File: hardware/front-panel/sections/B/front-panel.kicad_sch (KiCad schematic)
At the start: 76 parts, among them J1 Conn_02x20_Odd_Even, J10 SMA, J11 SMA, J12 SMA, J13 SMA, J14 SMA, J15 SMA, J16 SMA, J17 SMA, J18 SMA, J19 SMA, J2 Conn_02x20_Odd_Even, J20 SMA, J21 SMA, J22 SMA, J23 SMA, J24 SMA, J25 SMA, J3 Conn_02x20_Odd_Even, J30 OLED 0.96in module on 1x4 soc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, J31 KF128-2.54-10P, J32 KF128-5.0-2P, J33 Qwiic (vertical), J40 Module header 2x6 (shrouded), J411 KF301-5.0-2P, J412 KF301-5.0-2P, Q411 MMBT5551, Q412 MMBT5551, Q421 MMBT5551, Q422 MMBT5551, U401 6N137S-TA1-L, U402 6N137S-TA1-L, U410 SN74AHCT541PWR

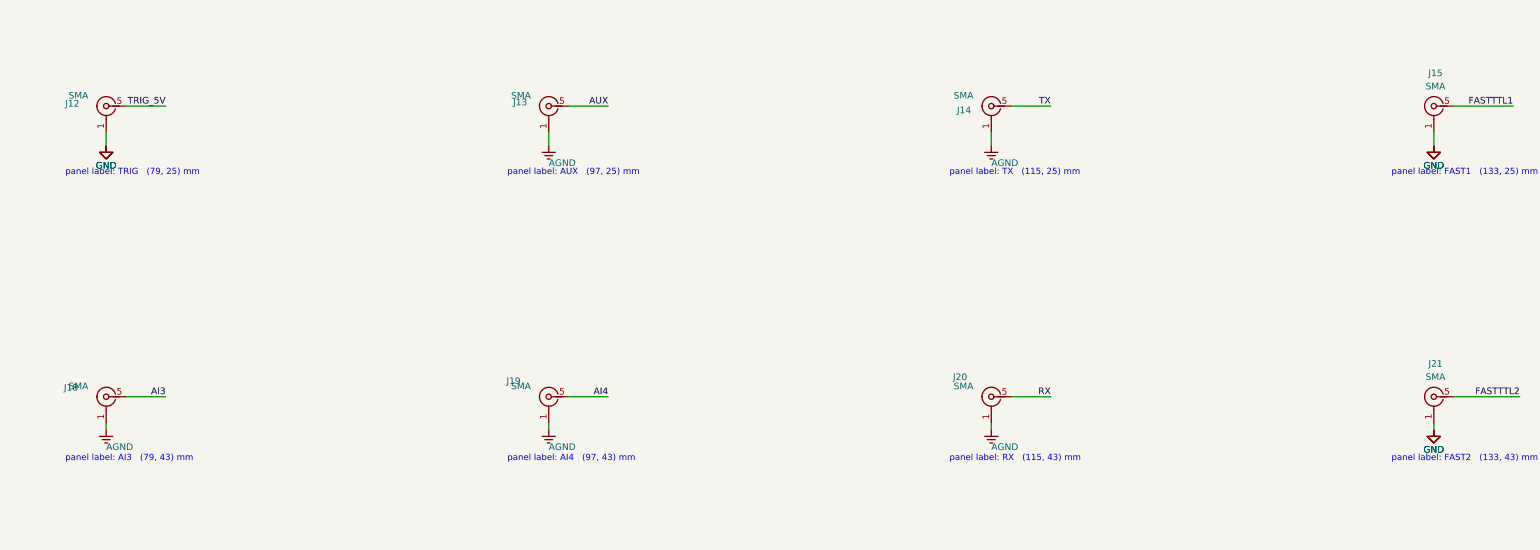
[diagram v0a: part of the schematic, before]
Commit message: Sections re-split from the instructor's 2026-09-25 masters (panel complete: 0 unconnected; main board 73 unconnected)
Co-Authored-By: Claude Fable 5.1 <noreply@anthropic.com>
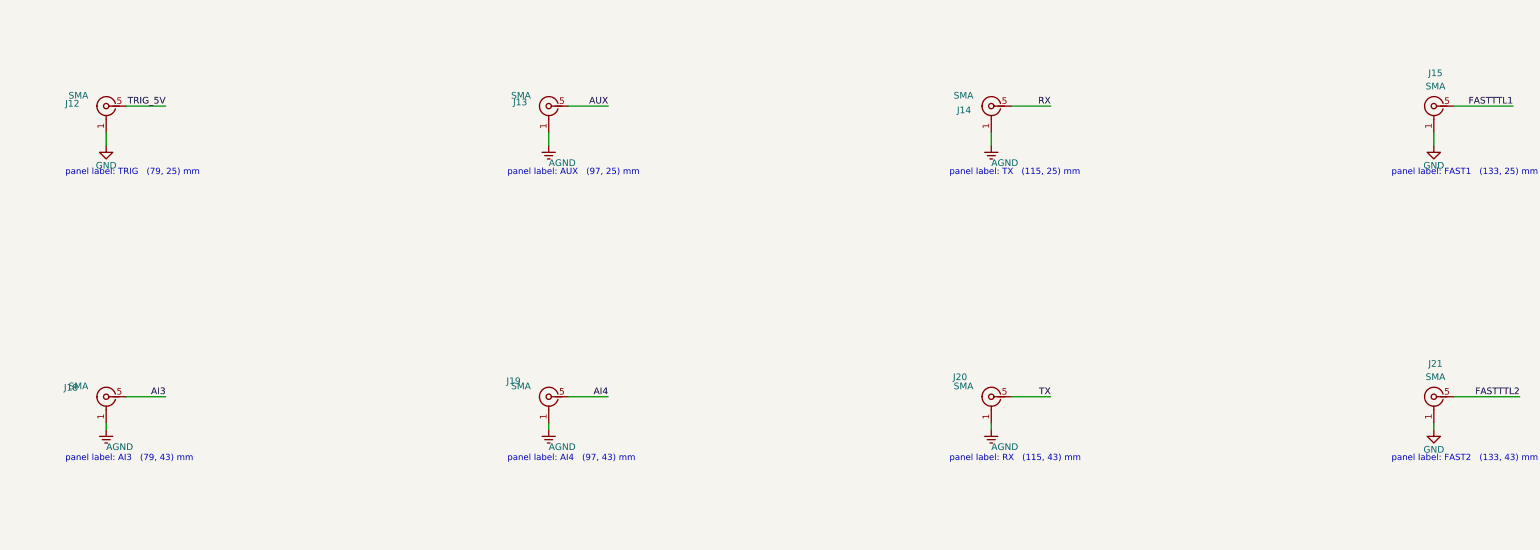
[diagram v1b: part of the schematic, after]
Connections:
- net RX: now also J14.5 (SIG); no longer J20.5 (SIG)
- net TX: now also J20.5 (SIG); no longer J14.5 (SIG)
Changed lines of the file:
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@@
 		)
 	)
-	(label "TX"
+	(label "RX"
 		(at 411.48 209.55 180)
 		(effects
@@
 		)
 	)
-	(label "RX"
+	(label "TX"
 		(at 411.48 265.43 180)
 		(effects
@@
 	)
 	(symbol
-		(lib_id "class_board:PWR_GND")
-		(at 229.87 217.17 0)
-		(unit 1)
-		(body_style 1)
-		(exclude_from_sim no)
-		(in_bom no)
-		(on_board yes)
-		(in_pos_files yes)
-		(dnp no)
-		(fields_autoplaced yes)
-		(property "Reference" "#PWR0285"
-			(at 227.33 213.868 0)
-			(hide yes)
-			(show_name no)
-			(do_not_autoplace no)
-			(effects
-				(font
-					(size 1.27 1.27)
-				)
-				(justify left bottom)
-			)
-		)
-		(property "Value" "GND"
-			(at 229.87 220.98 0)
-			(show_name no)
-			(do_not_autoplace no)
-			(effects
-				(font
-					(size 1.27 1.27)
-				)
-			)
-		)
-		(property "Footprint" ""
-			(at 229.87 217.17 0)
-			(hide yes)
-			(show_name no)
-			(do_not_autoplace no)
-			(effects
-				(font
-					(size 1.27 1.27)
-				)
-			)
-		)
-		(property "Datasheet" ""
-			(at 229.87 217.17 0)
-			(hide yes)
-			(show_name no)
-			(do_not_autoplace no)
-			(effects
-				(font
-					(size 1.27 1.27)
-				)
-			)
-		)
-		(property "Description" "Power symbol: GND"
-			(at 229.87 217.17 0)
-			(hide yes)
-			(show_name no)
-			(do_not_autoplace no)
-			(effects
-				(font
-					(size 1.27 1.27)
-				)
-			)
-		)
-		(pin "1"
-		)
-		(instances
-			(project "front-panel"
-				(path "/8e47bc66-3933-5476-97da-e27d85ee393b"
-					(reference "#PWR0285")
-					(unit 1)
-				)
-			)
-		)
-	)
-	(symbol
 		(lib_id "class_board:BWSMA-KE-Z001")
 		(at 400.05 265.43 0)
@@
 	)
 	(symbol
-		(lib_id "class_board:PWR_GND")
-		(at 485.14 271.78 0)
-		(unit 1)
-		(body_style 1)
-		(exclude_from_sim no)
-		(in_bom no)
-		(on_board yes)
-		(in_pos_files yes)
-		(dnp no)
-		(fields_autoplaced yes)
-		(property "Reference" "#PWR0287"
-			(at 482.6 268.478 0)
-			(hide yes)
-			(show_name no)
-			(do_not_autoplace no)
-			(effects
-				(font
-					(size 1.27 1.27)
-				)
-				(justify left bottom)
-			)
-		)
-		(property "Value" "GND"
-			(at 485.14 275.59 0)
-			(show_name no)
-			(do_not_autoplace no)
-			(effects
-				(font
-					(size 1.27 1.27)
-				)
-			)
-		)
-		(property "Footprint" ""
-			(at 485.14 271.78 0)
-			(hide yes)
-			(show_name no)
-			(do_not_autoplace no)
-			(effects
-				(font
-					(size 1.27 1.27)
-				)
-			)
-		)
-		(property "Datasheet" ""
-			(at 485.14 271.78 0)
-			(hide yes)
-			(show_name no)
-			(do_not_autoplace no)
-			(effects
-				(font
-					(size 1.27 1.27)
-				)
-			)
-		)
-		(property "Description" "Power symbol: GND"
-			(at 485.14 271.78 0)
-			(hide yes)
-			(show_name no)
-			(do_not_autoplace no)
-			(effects
-				(font
-					(size 1.27 1.27)
-				)
-			)
-		)
-		(pin "1"
-		)
-		(instances
-			(project "front-panel"
-				(path "/8e47bc66-3933-5476-97da-e27d85ee393b"
-					(reference "#PWR0287")
-					(unit 1)
-				)
-			)
-		)
-	)
-	(symbol
 		(lib_id "Connector_Generic:Conn_02x20_Odd_Even")
 		(at 398.78 92.71 0)
@@
 					(unit 1)
 				)
-			)
-		)
-	)
-	(symbol
-		(lib_id "class_board:PWR_GND")
-		(at 485.14 217.17 0)
-		(unit 1)
-		(body_style 1)
-		(exclude_from_sim no)
-		(in_bom no)
-		(on_board yes)
-		(in_pos_files yes)
-		(dnp no)
-		(fields_autoplaced yes)
-		(property "Reference" "#PWR0286"
-			(at 482.6 213.868 0)
-			(hide yes)
-			(show_name no)
-			(do_not_autoplace no)
-			(effects
-				(font
-					(size 1.27 1.27)
-				)
-				(justify left bottom)
-			)
-		)
-		(property "Value" "GND"
-			(at 485.14 220.98 0)
-			(show_name no)
-			(do_not_autoplace no)
-			(effects
-				(font
-					(size 1.27 1.27)
-				)
-			)
-		)
-		(property "Footprint" ""
-			(at 485.14 217.17 0)
-			(hide yes)
-			(show_name no)
-			(do_not_autoplace no)
-			(effects
-				(font
-					(size 1.27 1.27)
-				)
-			)
-		)
-		(property "Datasheet" ""
-			(at 485.14 217.17 0)
-			(hide yes)
-			(show_name no)
-			(do_not_autoplace no)
-			(effects
-				(font
-					(size 1.27 1.27)
-				)
-			)
-		)
-		(property "Description" "Power symbol: GND"
-			(at 485.14 217.17 0)
-			(hide yes)
-			(show_name no)
-			(do_not_autoplace no)
-			(effects
-				(font
-					(size 1.27 1.27)
-				)
-			)
-		)
-		(pin "1"
-		)
-		(instances
-			(project "front-panel"
-				(path "/8e47bc66-3933-5476-97da-e27d85ee393b"
-					(reference "#PWR0286")
-					(unit 1)
-				)
